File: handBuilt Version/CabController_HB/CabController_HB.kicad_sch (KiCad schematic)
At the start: 0 parts

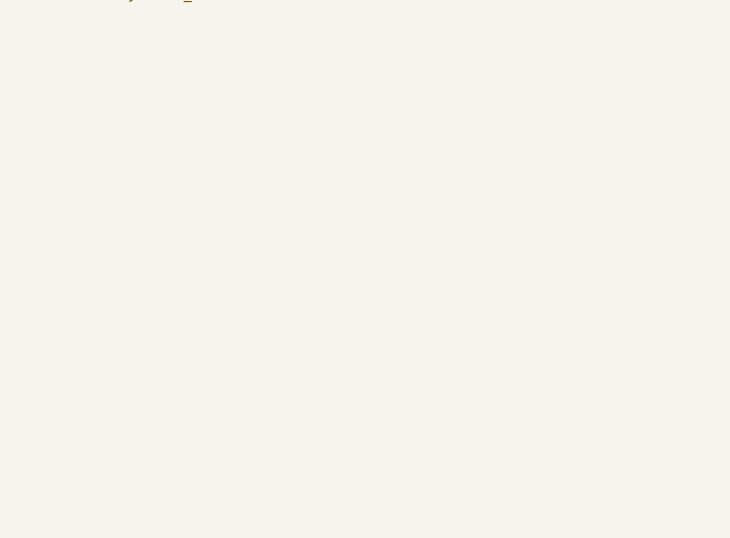
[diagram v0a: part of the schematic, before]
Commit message: new TDU V2 page
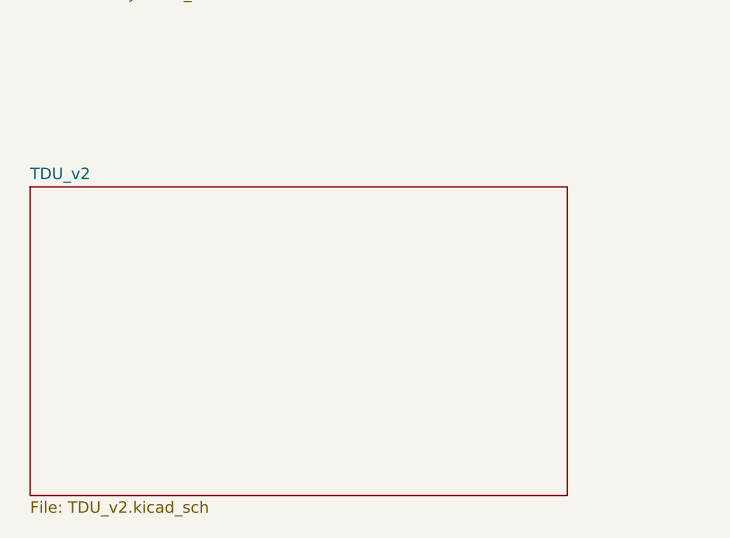
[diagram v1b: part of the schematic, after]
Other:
- added sheet TDU_v2 (TDU_v2.kicad_sch)
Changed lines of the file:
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@@
+	)
+	(sheet
+		(at 43.18 142.24)
+		(size 59.69 34.29)
+		(fields_autoplaced yes)
+		(stroke
+			(width 0.1524)
+			(type solid)
+		)
+		(fill
+			(color 0 0 0 0.0000)
+		)
+		(property "Sheetname" "TDU_v2"
+			(at 43.18 141.5284 0)
+			(effects
+				(font
+					(size 1.27 1.27)
+				)
+				(justify left bottom)
+			)
+		)
+		(property "Sheetfile" "TDU_v2.kicad_sch"
+			(at 43.18 177.1146 0)
+			(effects
+				(font
+					(size 1.27 1.27)
+				)
+				(justify left top)
+			)
+		)
+		(instances
+			(project "CabController_HB"
+				(path "/5c78a124-e1ff-4026-817c-c6044183edef"
+					(page "8")
+				)
+			)
+		)
 	)
 	(sheet
